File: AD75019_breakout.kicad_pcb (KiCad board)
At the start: 2 copper layers, 33 x 35.6 mm, 10 parts, among them P1 CONN_8, P2 CONN_8, P3 CONN_8X2, P4 CONN_8, U1 AD75019

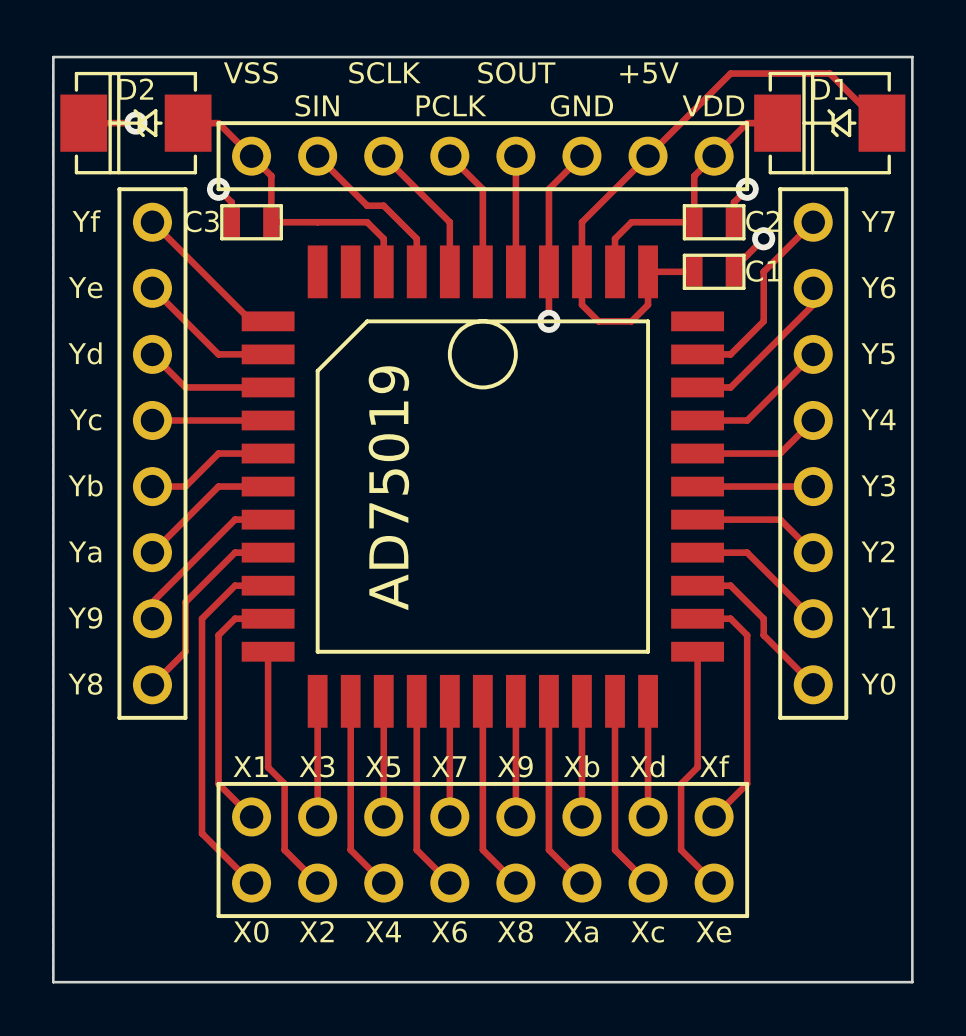
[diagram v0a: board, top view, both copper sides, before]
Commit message: AD75019 Rev2. case exploded labels.
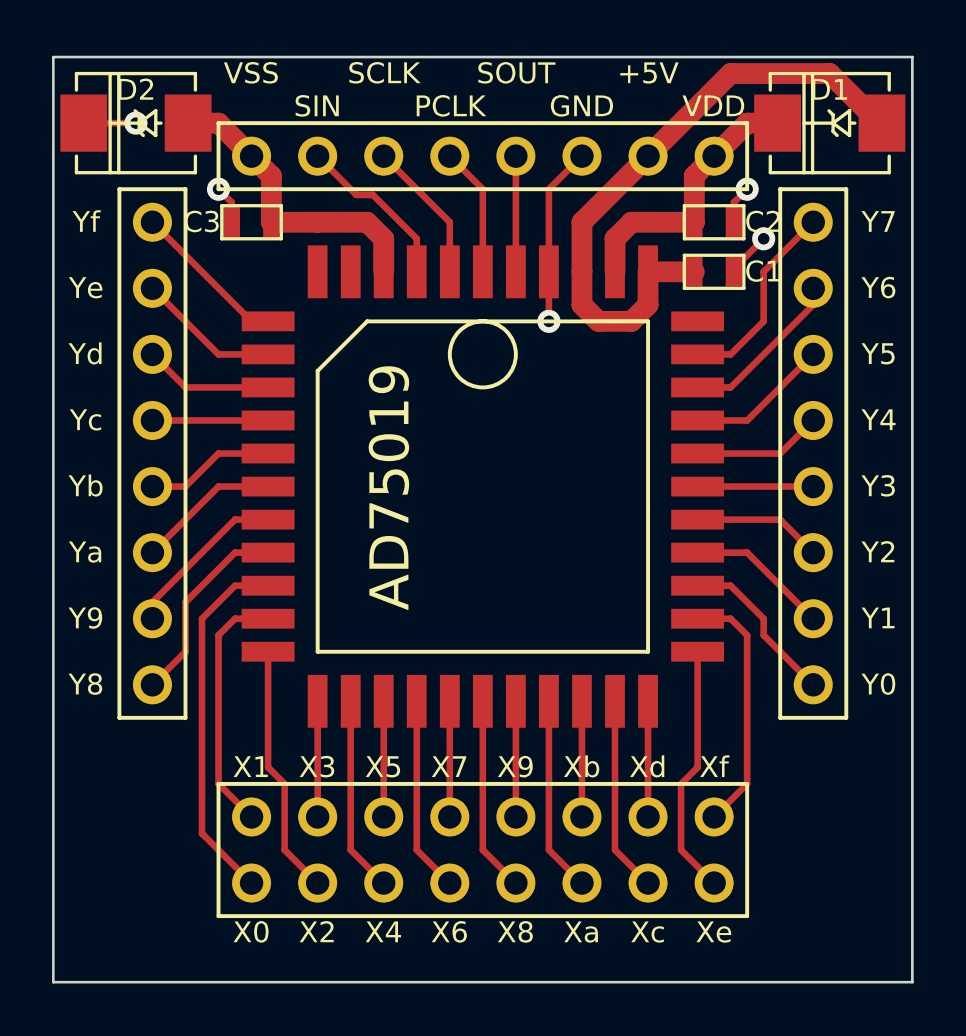
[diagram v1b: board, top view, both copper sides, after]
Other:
- net class fat added: clearance 0.254, trace_width 0.8, via_dia 0.889, via_drill 0.635
- board text added: "16x16 Crosspoint Switch AD75019 Breakout Rev2 -------------------- Licensed under CERN OHL v.1.2 by Open Music Kontrollers www.open-music-kontrollers.ch"
- board text removed: "16x16 Crosspoint Switch AD75019 Breakout Rev1 -------------------- Licensed under CERN OHL v.1.2 by Open Music Kontrollers www.open-music-kontrollers.ch"
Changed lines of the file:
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@@
     (nets 41)
   )
-  (page A3)
+  (page User 150.012 110.007)
+  (title_block
+    (title "AD75019 16x16 CrossSwitch Breakout")
+    (rev 2)
+    (company "by Open Music Kontrollers (www.open-music-kontrollers.ch)")
+    (comment 1 "Licensed under CERN OHL v.1.2")
+    (comment 2 "Copyright (c) 2013 Hanspeter Portner (dev@open-music-kontrollers.ch)")
+  )
   (layers
     (15 F.Cu signal)
@@
     (uvia_drill 0.127)
     (add_net "")
-    (add_net +12V)
-    (add_net +5V)
-    (add_net -12V)
     (add_net GND)
     (add_net N-000001)
@@
     (add_net N-000009)
   )
+  (net_class fat ""
+    (clearance 0.254)
+    (trace_width 0.8)
+    (via_dia 0.889)
+    (via_drill 0.635)
+    (uvia_dia 0.508)
+    (uvia_drill 0.127)
+    (add_net +12V)
+    (add_net +5V)
+    (add_net -12V)
+  )
   (module SIL-8x2 (layer F.Cu)
     (at 29.21 44.45)
@@
     )
   )
-  (gr_text "16x16 Crosspoint Switch\nAD75019 Breakout Rev1\n--------------------\nLicensed under CERN OHL v.1.2\nby Open Music Kontrollers\nwww.open-music-kontrollers.ch" (at 38.1 24.765) (layer B.SilkS)
+  (gr_text "16x16 Crosspoint Switch\nAD75019 Breakout Rev2\n--------------------\nLicensed under CERN OHL v.1.2\nby Open Music Kontrollers\nwww.open-music-kontrollers.ch" (at 38.1 24.765) (layer B.SilkS)
     (effects (font (size 0.8 0.8) (thickness 0.2)) (justify left mirror))
   )
@@
     (effects (font (size 0.8 0.8) (thickness 0.2)))
   )
-  (segment (start 40.5384 15.24) (end 39.37 15.24) (width 0.254) (layer F.Cu) (net 1))
-  (segment (start 39.37 15.24) (end 38.1 16.51) (width 0.254) (layer F.Cu) (net 1))
-  (segment (start 37.338 19.05) (end 37.338 17.272) (width 0.254) (layer F.Cu) (net 1))
-  (segment (start 37.338 17.272) (end 38.1 16.51) (width 0.254) (layer F.Cu) (net 1))
-  (segment (start 34.925 19.05) (end 37.338 19.05) (width 0.254) (layer F.Cu) (net 1))
-  (segment (start 34.29 20.955) (end 34.29 19.685) (width 0.254) (layer F.Cu) (net 1))
-  (segment (start 34.29 19.685) (end 34.925 19.05) (width 0.254) (layer F.Cu) (net 1))
+  (segment (start 40.5384 15.24) (end 39.37 15.24) (width 0.8) (layer F.Cu) (net 1))
+  (segment (start 39.37 15.24) (end 38.1 16.51) (width 0.8) (layer F.Cu) (net 1))
+  (segment (start 37.338 19.05) (end 37.338 17.272) (width 0.8) (layer F.Cu) (net 1))
+  (segment (start 37.338 17.272) (end 38.1 16.51) (width 0.8) (layer F.Cu) (net 1))
+  (segment (start 34.925 19.05) (end 37.338 19.05) (width 0.8) (layer F.Cu) (net 1))
+  (segment (start 34.29 20.955) (end 34.29 19.685) (width 0.8) (layer F.Cu) (net 1))
+  (segment (start 34.29 19.685) (end 34.925 19.05) (width 0.8) (layer F.Cu) (net 1))
   (segment (start 44.5516 15.24) (end 44.45 15.24) (width 0.254) (layer F.Cu) (net 2))
-  (segment (start 38.735 13.335) (end 35.56 16.51) (width 0.254) (layer F.Cu) (net 2))
-  (segment (start 42.545 13.335) (end 38.735 13.335) (width 0.254) (layer F.Cu) (net 2))
-  (segment (start 44.45 15.24) (end 42.545 13.335) (width 0.254) (layer F.Cu) (net 2))
-  (segment (start 37.338 20.955) (end 35.56 20.955) (width 0.254) (layer F.Cu) (net 2))
-  (segment (start 33.02 20.955) (end 33.02 22.225) (width 0.254) (layer F.Cu) (net 2))
-  (segment (start 35.56 22.225) (end 35.56 20.955) (width 0.254) (layer F.Cu) (net 2))
-  (segment (start 34.925 22.86) (end 35.56 22.225) (width 0.254) (layer F.Cu) (net 2))
-  (segment (start 33.655 22.86) (end 34.925 22.86) (width 0.254) (layer F.Cu) (net 2))
-  (segment (start 33.02 22.225) (end 33.655 22.86) (width 0.254) (layer F.Cu) (net 2))
-  (segment (start 33.02 20.955) (end 33.02 19.05) (width 0.254) (layer F.Cu) (net 2))
-  (segment (start 33.02 19.05) (end 35.56 16.51) (width 0.254) (layer F.Cu) (net 2))
-  (segment (start 17.8816 15.24) (end 19.05 15.24) (width 0.254) (layer F.Cu) (net 3))
-  (segment (start 19.05 15.24) (end 20.32 16.51) (width 0.254) (layer F.Cu) (net 3))
-  (segment (start 21.082 19.05) (end 21.082 17.272) (width 0.254) (layer F.Cu) (net 3))
-  (segment (start 21.082 17.272) (end 20.32 16.51) (width 0.254) (layer F.Cu) (net 3))
-  (segment (start 22.86 19.05) (end 21.082 19.05) (width 0.254) (layer F.Cu) (net 3))
-  (segment (start 25.4 20.955) (end 25.4 19.685) (width 0.254) (layer F.Cu) (net 3))
-  (segment (start 24.765 19.05) (end 22.86 19.05) (width 0.254) (layer F.Cu) (net 3))
-  (segment (start 25.4 19.685) (end 24.765 19.05) (width 0.254) (layer F.Cu) (net 3))
+  (segment (start 38.735 13.335) (end 35.56 16.51) (width 0.8) (layer F.Cu) (net 2))
+  (segment (start 42.545 13.335) (end 38.735 13.335) (width 0.8) (layer F.Cu) (net 2))
+  (segment (start 44.45 15.24) (end 42.545 13.335) (width 0.8) (layer F.Cu) (net 2))
+  (segment (start 37.338 20.955) (end 35.56 20.955) (width 0.8) (layer F.Cu) (net 2))
+  (segment (start 33.02 20.955) (end 33.02 22.225) (width 0.8) (layer F.Cu) (net 2))
+  (segment (start 35.56 22.225) (end 35.56 20.955) (width 0.8) (layer F.Cu) (net 2))
+  (segment (start 34.925 22.86) (end 35.56 22.225) (width 0.8) (layer F.Cu) (net 2))
+  (segment (start 33.655 22.86) (end 34.925 22.86) (width 0.8) (layer F.Cu) (net 2))
+  (segment (start 33.02 22.225) (end 33.655 22.86) (width 0.8) (layer F.Cu) (net 2))
+  (segment (start 33.02 20.955) (end 33.02 19.05) (width 0.8) (layer F.Cu) (net 2))
+  (segment (start 33.02 19.05) (end 35.56 16.51) (width 0.8) (layer F.Cu) (net 2))
+  (segment (start 17.8816 15.24) (end 19.05 15.24) (width 0.8) (layer F.Cu) (net 3))
+  (segment (start 19.05 15.24) (end 20.32 16.51) (width 0.8) (layer F.Cu) (net 3))
+  (segment (start 21.082 19.05) (end 21.082 17.272) (width 0.8) (layer F.Cu) (net 3))
+  (segment (start 21.082 17.272) (end 20.32 16.51) (width 0.8) (layer F.Cu) (net 3))
+  (segment (start 22.86 19.05) (end 21.082 19.05) (width 0.8) (layer F.Cu) (net 3))
+  (segment (start 25.4 20.955) (end 25.4 19.685) (width 0.8) (layer F.Cu) (net 3))
+  (segment (start 24.765 19.05) (end 22.86 19.05) (width 0.8) (layer F.Cu) (net 3))
+  (segment (start 25.4 19.685) (end 24.765 19.05) (width 0.8) (layer F.Cu) (net 3))
   (segment (start 38.862 20.955) (end 38.862 20.828) (width 0.254) (layer F.Cu) (net 4))
   (via (at 40.005 19.685) (size 0.889) (layers F.Cu B.Cu) (net 4))
@@
   (segment (start 40.64 30.48) (end 41.91 31.75) (width 0.254) (layer F.Cu) (net 14))
   (segment (start 26.67 20.955) (end 26.67 19.685) (width 0.254) (layer F.Cu) (net 15))
-  (segment (start 24.765 18.415) (end 22.86 16.51) (width 0.254) (layer F.Cu) (net 15))
-  (segment (start 25.4 18.415) (end 24.765 18.415) (width 0.254) (layer F.Cu) (net 15))
-  (segment (start 26.67 19.685) (end 25.4 18.415) (width 0.254) (layer F.Cu) (net 15))
+  (segment (start 24.35 18) (end 22.86 16.51) (width 0.254) (layer F.Cu) (net 15))
+  (segment (start 24.985 18) (end 24.35 18) (width 0.254) (layer F.Cu) (net 15))
+  (segment (start 26.67 19.685) (end 24.985 18) (width 0.254) (layer F.Cu) (net 15))
   (segment (start 16.51 36.83) (end 17.78 35.56) (width 0.254) (layer F.Cu) (net 16))
   (segment (start 19.685 31.75) (end 20.955 31.75) (width 0.254) (layer F.Cu) (net 16))
